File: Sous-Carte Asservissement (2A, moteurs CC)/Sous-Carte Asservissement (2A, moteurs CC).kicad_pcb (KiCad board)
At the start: 2 copper layers, 6 parts, among them P1 CONN_01X18, P2 CONN_01X02, P3 CONN_01X02, P4 CONN_01X04, P5 CONN_01X04

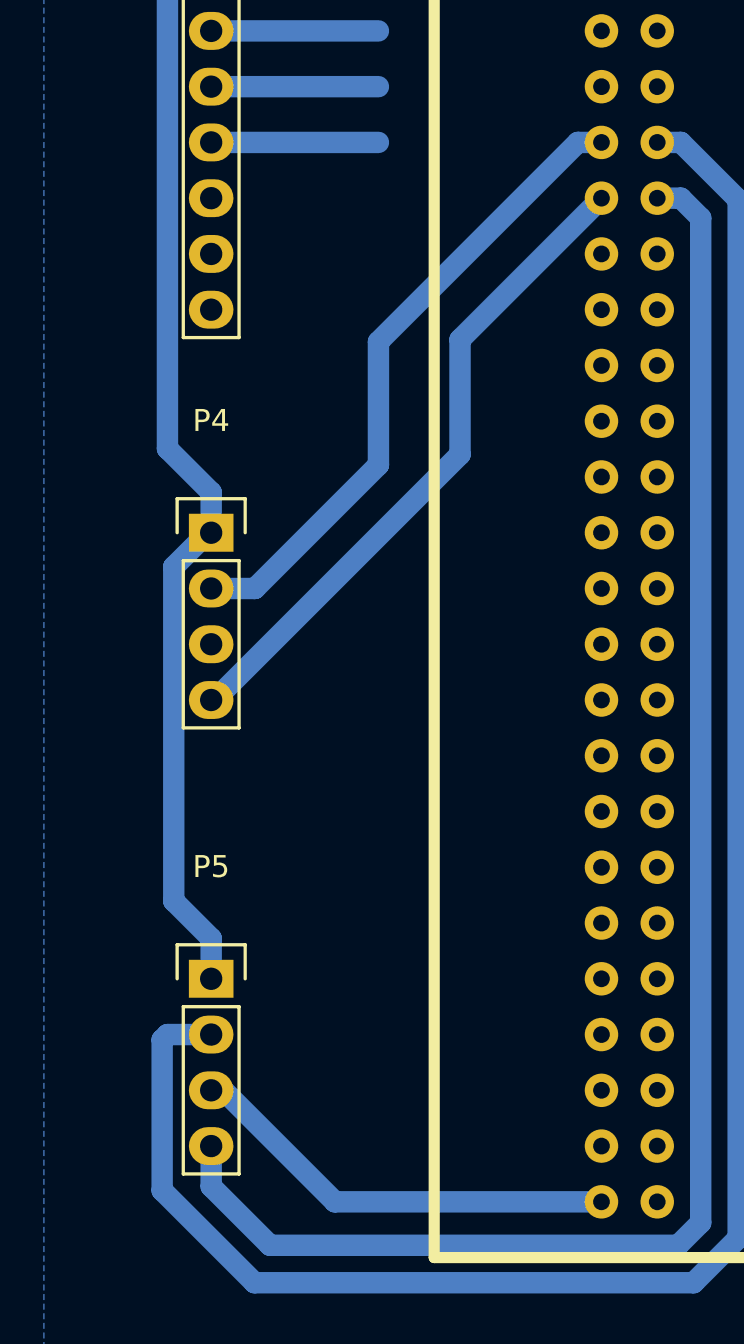
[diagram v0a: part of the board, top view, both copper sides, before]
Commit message: changé de timer un codeur
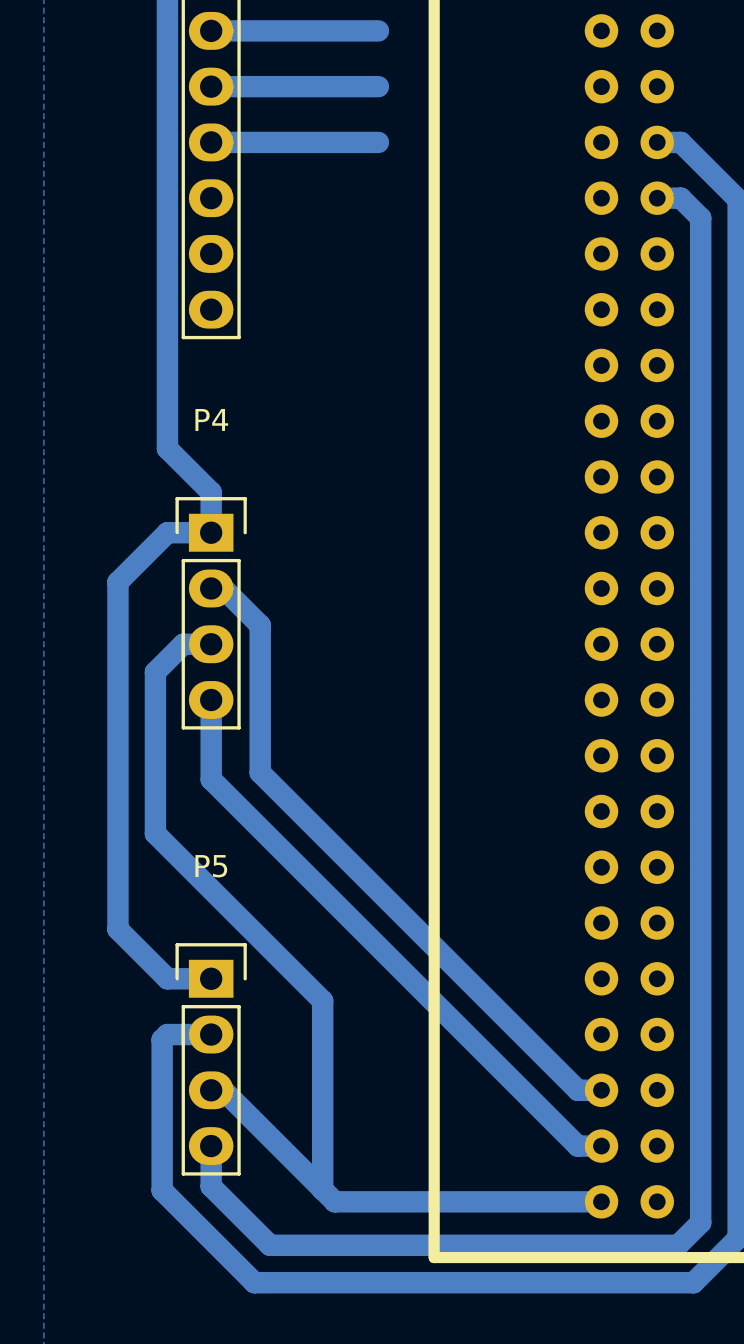
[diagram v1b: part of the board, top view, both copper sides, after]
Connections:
- P4 pad 2: TIM5_CH2 -> TIM4_CH2
- P4 pad 4: TIM5_CH4 -> TIM4_CH4
- stm321 pad 45: Net-(stm321-Pad45) -> TIM4_CH2
- stm321 pad 47: Net-(stm321-Pad47) -> TIM4_CH4
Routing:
- net TIM4_CH2: track 0.00 -> 31.2 mm
- net TIM5_CH4: track 30.3 -> 0.00 mm
- net GND: track 20.0 -> 49.8 mm
- net TIM5_CH2: track 29.5 -> 0.00 mm
- net TIM4_CH4: track 0.00 -> 28.5 mm
- net +5V: track 150.5 -> 155.0 mm

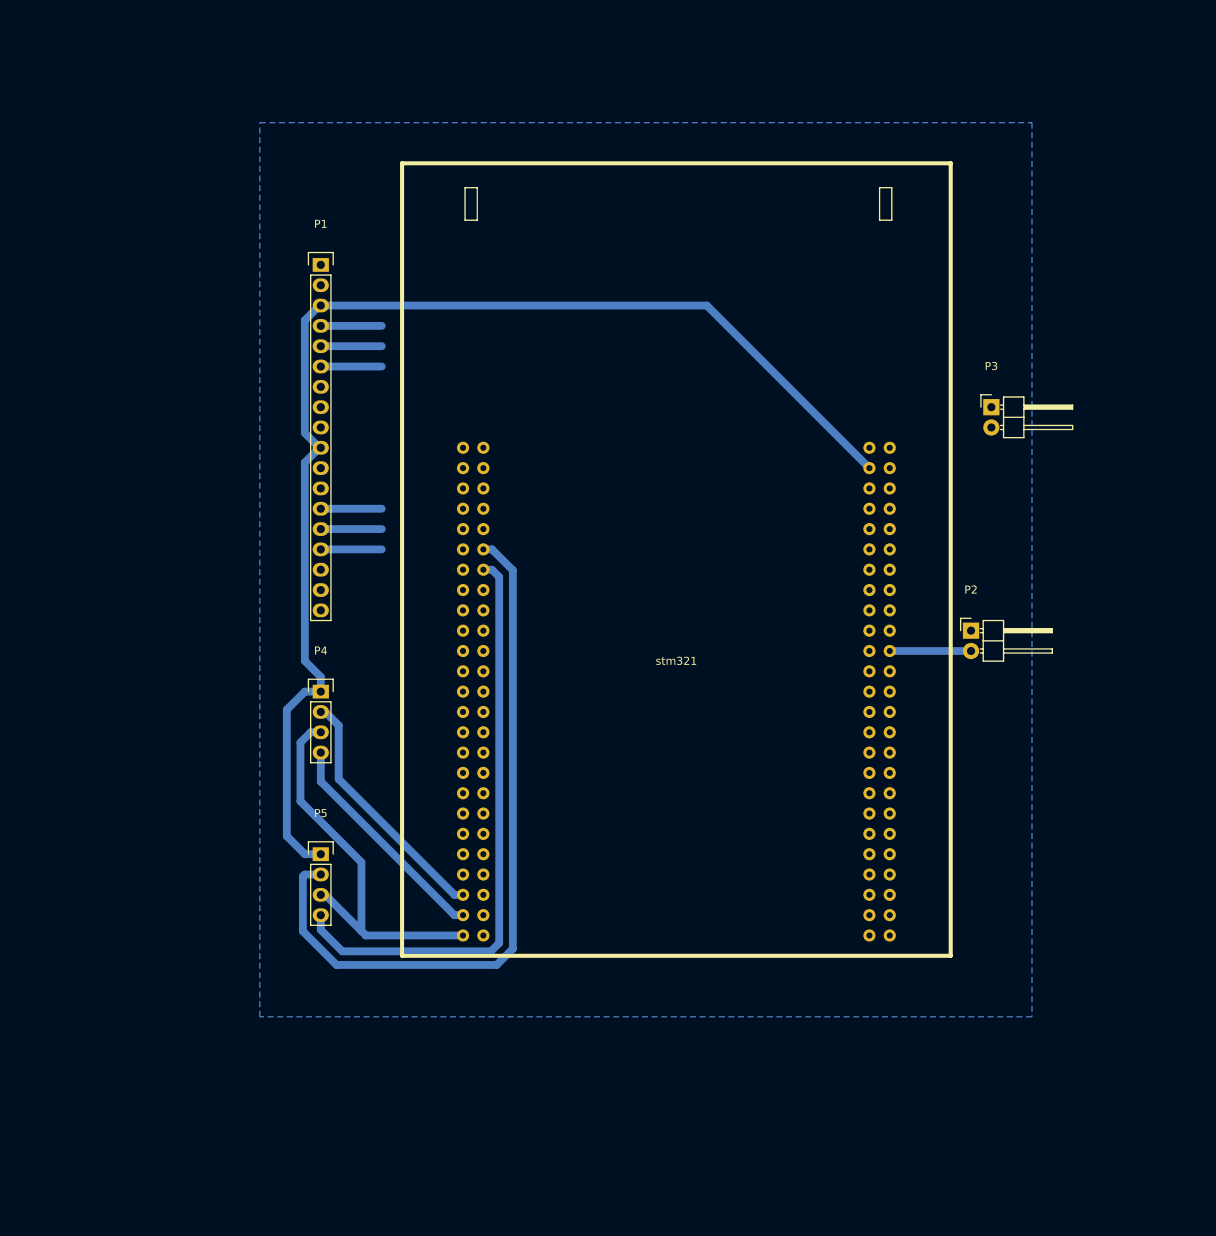
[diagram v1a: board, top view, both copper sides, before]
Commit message: Sous carte asser dite -- arraignée - avec pinoche et tout, routée
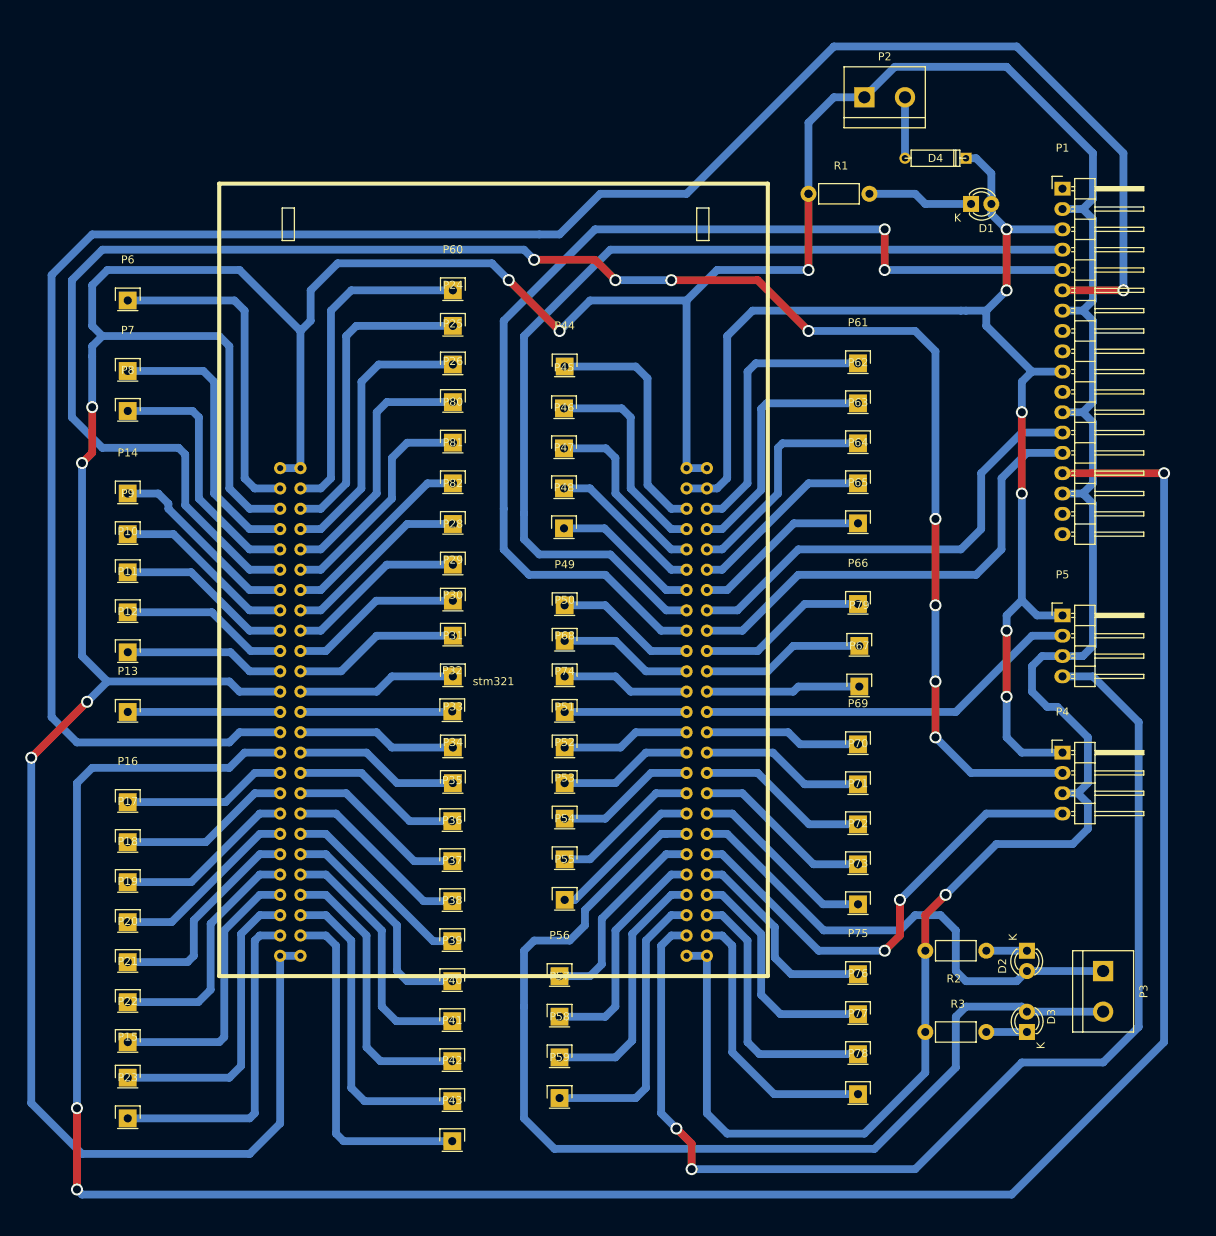
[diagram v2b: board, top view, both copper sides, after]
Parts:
- added D1: LED, LEDs:LED-3MM, F.Cu at (172.7, 55.9)
- added D2: LED, LEDs:LED-3MM, F.Cu at (179.7, 149.2)
- added D3: LED, LEDs:LED-3MM, F.Cu at (179.7, 159.4)
- added D4: D, Discret:D3, F.Cu at (168.3, 50.2)
- added P10: CONN_01X01, Pin_Headers:Pin_Header_Straight_1x01, F.Cu at (67.3, 101.9)
- added P11: CONN_01X01, Pin_Headers:Pin_Header_Straight_1x01, F.Cu at (67.3, 106.9)
- added P12: CONN_01X01, Pin_Headers:Pin_Header_Straight_1x01, F.Cu at (67.3, 111.9)
- added P13: CONN_01X01, Pin_Headers:Pin_Header_Straight_1x01, F.Cu at (67.3, 119.4)
- added P14: CONN_01X01, Pin_Headers:Pin_Header_Straight_1x01, F.Cu at (67.3, 92.1)
- added P15: CONN_01X01, Pin_Headers:Pin_Header_Straight_1x01, F.Cu at (67.3, 165.1)
- added P16: CONN_01X01, Pin_Headers:Pin_Header_Straight_1x01, F.Cu at (67.3, 130.6)
- added P17: CONN_01X01, Pin_Headers:Pin_Header_Straight_1x01, F.Cu at (67.3, 135.6)
- added P18: CONN_01X01, Pin_Headers:Pin_Header_Straight_1x01, F.Cu at (67.3, 140.6)
- added P19: CONN_01X01, Pin_Headers:Pin_Header_Straight_1x01, F.Cu at (67.3, 145.6)
- added P20: CONN_01X01, Pin_Headers:Pin_Header_Straight_1x01, F.Cu at (67.3, 150.6)
- added P21: CONN_01X01, Pin_Headers:Pin_Header_Straight_1x01, F.Cu at (67.3, 155.6)
- added P22: CONN_01X01, Pin_Headers:Pin_Header_Straight_1x01, F.Cu at (67.3, 160.6)
- added P23: CONN_01X01, Pin_Headers:Pin_Header_Straight_1x01, F.Cu at (67.3, 170.2)
- added P24: CONN_01X01, Pin_Headers:Pin_Header_Straight_1x01, F.Cu at (108.0, 71.1)
- added P25: CONN_01X01, Pin_Headers:Pin_Header_Straight_1x01, F.Cu at (108.0, 76.0)
- added P26: CONN_01X01, Pin_Headers:Pin_Header_Straight_1x01, F.Cu at (108.0, 80.6)
- added P28: CONN_01X01, Pin_Headers:Pin_Header_Straight_1x01, F.Cu at (108.0, 101.0)
- added P29: CONN_01X01, Pin_Headers:Pin_Header_Straight_1x01, F.Cu at (108.0, 105.5)
- added P30: CONN_01X01, Pin_Headers:Pin_Header_Straight_1x01, F.Cu at (108.0, 109.9)
- added P31: CONN_01X01, Pin_Headers:Pin_Header_Straight_1x01, F.Cu at (108.0, 114.9)
- added P32: CONN_01X01, Pin_Headers:Pin_Header_Straight_1x01, F.Cu at (107.9, 119.3)
- added P33: CONN_01X01, Pin_Headers:Pin_Header_Straight_1x01, F.Cu at (108.0, 123.8)
- added P34: CONN_01X01, Pin_Headers:Pin_Header_Straight_1x01, F.Cu at (108.0, 128.3)
- added P35: CONN_01X01, Pin_Headers:Pin_Header_Straight_1x01, F.Cu at (107.9, 133.0)
- added P36: CONN_01X01, Pin_Headers:Pin_Header_Straight_1x01, F.Cu at (107.9, 138.0)
- added P37: CONN_01X01, Pin_Headers:Pin_Header_Straight_1x01, F.Cu at (107.9, 143.0)
- added P38: CONN_01X01, Pin_Headers:Pin_Header_Straight_1x01, F.Cu at (107.9, 148.0)
- added P39: CONN_01X01, Pin_Headers:Pin_Header_Straight_1x01, F.Cu at (107.9, 153.0)
- added P40: CONN_01X01, Pin_Headers:Pin_Header_Straight_1x01, F.Cu at (107.9, 158.0)
- added P41: CONN_01X01, Pin_Headers:Pin_Header_Straight_1x01, F.Cu at (107.9, 163.0)
- added P42: CONN_01X01, Pin_Headers:Pin_Header_Straight_1x01, F.Cu at (107.9, 168.0)
- added P43: CONN_01X01, Pin_Headers:Pin_Header_Straight_1x01, F.Cu at (107.9, 173.0)
- added P44: CONN_01X01, Pin_Headers:Pin_Header_Straight_1x01, F.Cu at (121.9, 76.2)
- added P45: CONN_01X01, Pin_Headers:Pin_Header_Straight_1x01, F.Cu at (121.8, 81.4)
- added P46: CONN_01X01, Pin_Headers:Pin_Header_Straight_1x01, F.Cu at (121.8, 86.4)
- added P47: CONN_01X01, Pin_Headers:Pin_Header_Straight_1x01, F.Cu at (121.8, 91.4)
- added P48: CONN_01X01, Pin_Headers:Pin_Header_Straight_1x01, F.Cu at (121.8, 96.4)
- added P49: CONN_01X01, Pin_Headers:Pin_Header_Straight_1x01, F.Cu at (121.9, 106.0)
- added P50: CONN_01X01, Pin_Headers:Pin_Header_Straight_1x01, F.Cu at (121.9, 110.5)
- added P51: CONN_01X01, Pin_Headers:Pin_Header_Straight_1x01, F.Cu at (121.9, 123.8)
- added P52: CONN_01X01, Pin_Headers:Pin_Header_Straight_1x01, F.Cu at (121.9, 128.3)
- added P53: CONN_01X01, Pin_Headers:Pin_Header_Straight_1x01, F.Cu at (121.9, 132.7)
- added P54: CONN_01X01, Pin_Headers:Pin_Header_Straight_1x01, F.Cu at (121.9, 137.8)
- added P55: CONN_01X01, Pin_Headers:Pin_Header_Straight_1x01, F.Cu at (121.9, 142.9)
- added P56: CONN_01X01, Pin_Headers:Pin_Header_Straight_1x01, F.Cu at (121.3, 152.4)
- added P57: CONN_01X01, Pin_Headers:Pin_Header_Straight_1x01, F.Cu at (121.3, 157.5)
- added P58: CONN_01X01, Pin_Headers:Pin_Header_Straight_1x01, F.Cu at (121.3, 162.6)
- added P59: CONN_01X01, Pin_Headers:Pin_Header_Straight_1x01, F.Cu at (121.3, 167.6)
- added P6: CONN_01X01, Pin_Headers:Pin_Header_Straight_1x01, F.Cu at (67.3, 67.9)
- added P60: CONN_01X01, Pin_Headers:Pin_Header_Straight_1x01, F.Cu at (108.0, 66.7)
- added P61: CONN_01X01, Pin_Headers:Pin_Header_Straight_1x01, F.Cu at (158.6, 75.8)
- added P62: CONN_01X01, Pin_Headers:Pin_Header_Straight_1x01, F.Cu at (158.6, 80.8)
- added P63: CONN_01X01, Pin_Headers:Pin_Header_Straight_1x01, F.Cu at (158.6, 85.8)
- added P64: CONN_01X01, Pin_Headers:Pin_Header_Straight_1x01, F.Cu at (158.6, 90.8)
- added P65: CONN_01X01, Pin_Headers:Pin_Header_Straight_1x01, F.Cu at (158.6, 95.8)
- added P66: CONN_01X01, Pin_Headers:Pin_Header_Straight_1x01, F.Cu at (158.6, 105.9)
- added P67: CONN_01X01, Pin_Headers:Pin_Header_Straight_1x01, F.Cu at (158.8, 116.2)
- added P68: CONN_01X01, Pin_Headers:Pin_Header_Straight_1x01, F.Cu at (121.9, 114.9)
- added P69: CONN_01X01, Pin_Headers:Pin_Header_Straight_1x01, F.Cu at (158.6, 123.4)
- added P7: CONN_01X01, Pin_Headers:Pin_Header_Straight_1x01, F.Cu at (67.3, 76.8)
- added P70: CONN_01X01, Pin_Headers:Pin_Header_Straight_1x01, F.Cu at (158.6, 128.4)
- added P71: CONN_01X01, Pin_Headers:Pin_Header_Straight_1x01, F.Cu at (158.6, 133.4)
- added P72: CONN_01X01, Pin_Headers:Pin_Header_Straight_1x01, F.Cu at (158.6, 138.4)
- added P73: CONN_01X01, Pin_Headers:Pin_Header_Straight_1x01, F.Cu at (158.6, 143.4)
- added P74: CONN_01X01, Pin_Headers:Pin_Header_Straight_1x01, F.Cu at (121.9, 119.4)
- added P75: CONN_01X01, Pin_Headers:Pin_Header_Straight_1x01, F.Cu at (158.6, 152.2)
- added P76: CONN_01X01, Pin_Headers:Pin_Header_Straight_1x01, F.Cu at (158.6, 157.2)
- added P77: CONN_01X01, Pin_Headers:Pin_Header_Straight_1x01, F.Cu at (158.6, 162.2)
- added P78: CONN_01X01, Pin_Headers:Pin_Header_Straight_1x01, F.Cu at (158.6, 167.2)
- added P79: CONN_01X01, Pin_Headers:Pin_Header_Straight_1x01, F.Cu at (158.8, 111.1)
- added P8: CONN_01X01, Pin_Headers:Pin_Header_Straight_1x01, F.Cu at (67.3, 81.8)
- added P80: CONN_01X01, Pin_Headers:Pin_Header_Straight_1x01, F.Cu at (108.0, 85.7)
- added P81: CONN_01X01, Pin_Headers:Pin_Header_Straight_1x01, F.Cu at (108.0, 90.8)
- added P82: CONN_01X01, Pin_Headers:Pin_Header_Straight_1x01, F.Cu at (108.0, 95.9)
- added P9: CONN_01X01, Pin_Headers:Pin_Header_Straight_1x01, F.Cu at (67.3, 97.2)
- added R1: 150, Resistors_ThroughHole:Resistor_Horizontal_RM7mm, F.Cu at (152.4, 54.6)
- added R2: 150, Resistors_ThroughHole:Resistor_Horizontal_RM7mm, F.Cu at (174.6, 149.2)
- added R3: 150, Resistors_ThroughHole:Resistor_Horizontal_RM7mm, F.Cu at (167.0, 159.4)
- P1: footprint Pin_Headers:Pin_Header_Straight_1x18 -> Pin_Headers:Pin_Header_Angled_1x18
- P2, P3: footprint Pin_Headers:Pin_Header_Angled_1x02 -> Connect:bornier2
- P4, P5: footprint Pin_Headers:Pin_Header_Straight_1x04 -> Pin_Headers:Pin_Header_Angled_1x04
- moved P5 97.4 mm to (184.2, 107.3)
- moved P1 93.2 mm to (184.2, 54.0)
- moved P4 93.0 mm to (184.2, 124.5)
- moved P3 74.3 mm to (189.2, 154.3), turned to 270 degrees
- moved P2 67.5 mm to (161.9, 42.5)
- moved stm321 23.0 mm to (86.4, 88.9)
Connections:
- P2 pad 2: +BATT -> Net-(D4-Pad2)
- P4 pad 2: TIM4_CH2 -> TIM2_CH2
- P4 pad 4: TIM4_CH4 -> TIM2_CH1
- P5 pad 2: TIM5_CH1 -> TIM3_CH2
- P5 pad 4: TIM5_CH3 -> TIM3_CH1
- stm321 pad 11: TIM5_CH2 -> TIM2_CH2
- stm321 pad 12: TIM5_CH1 -> Net-(P80-Pad1)
- stm321 pad 13: TIM5_CH4 -> Net-(P14-Pad1)
- stm321 pad 14: TIM5_CH3 -> Net-(P81-Pad1)
- stm321 pad 27: Net-(stm321-Pad27) -> M1PWM
- stm321 pad 29: Net-(stm321-Pad29) -> M2PWM
- stm321 pad 45: TIM4_CH2 -> Net-(P15-Pad1)
- stm321 pad 47: TIM4_CH4 -> Net-(P23-Pad1)
- stm321 pad 65: Net-(stm321-Pad65) -> M1I2
- stm321 pad 66: Net-(stm321-Pad66) -> M2_I2
- stm321 pad 67: Net-(stm321-Pad67) -> M1I1
- stm321 pad 68: Net-(stm321-Pad68) -> M2_I1
- stm321 pad 72: +BATT -> Net-(P79-Pad1)
- stm321 pad 76: Net-(stm321-Pad76) -> TIM3_CH2
- stm321 pad 87: Net-(stm321-Pad87) -> UART_TX
- stm321 pad 88: Net-(stm321-Pad88) -> UART_RX
- stm321 pad 90: Net-(stm321-Pad90) -> TIM2_CH1
- stm321 pad 97: Net-(stm321-Pad97) -> TIM3_CH1
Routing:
- net GND: track 49.8 -> 651.7 mm, vias 0 -> 9
- net M2PWM: track 7.62 -> 305.6 mm, vias 0 -> 3
- net M1PWM: track 7.62 -> 261.8 mm, vias 0 -> 1
- net TIM2_CH2: track 0.00 -> 235.6 mm, vias 0 -> 8
- net TIM3_CH1: track 0.00 -> 146.5 mm, vias 0 -> 2
- net UART_TX: track 0.00 -> 133.8 mm
- net M1I1: track 7.62 -> 135.3 mm, vias 0 -> 2
- net M1I2: track 7.62 -> 121.2 mm
- net TIM5_CH1: track 90.1 -> 0.00 mm
- net TIM5_CH3: track 73.8 -> 0.00 mm
- net UART_RX: track 0.00 -> 62.2 mm
- net TIM2_CH1: track 0.00 -> 59.2 mm, vias 0 -> 2
- net M2_I1: track 7.62 -> 58.9 mm
- net M2_I2: track 7.62 -> 57.7 mm
- net TIM3_CH2: track 0.00 -> 48.4 mm
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- removed copper zone on B.Cu, net GND

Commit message: Ajout pin_header Uart Asser
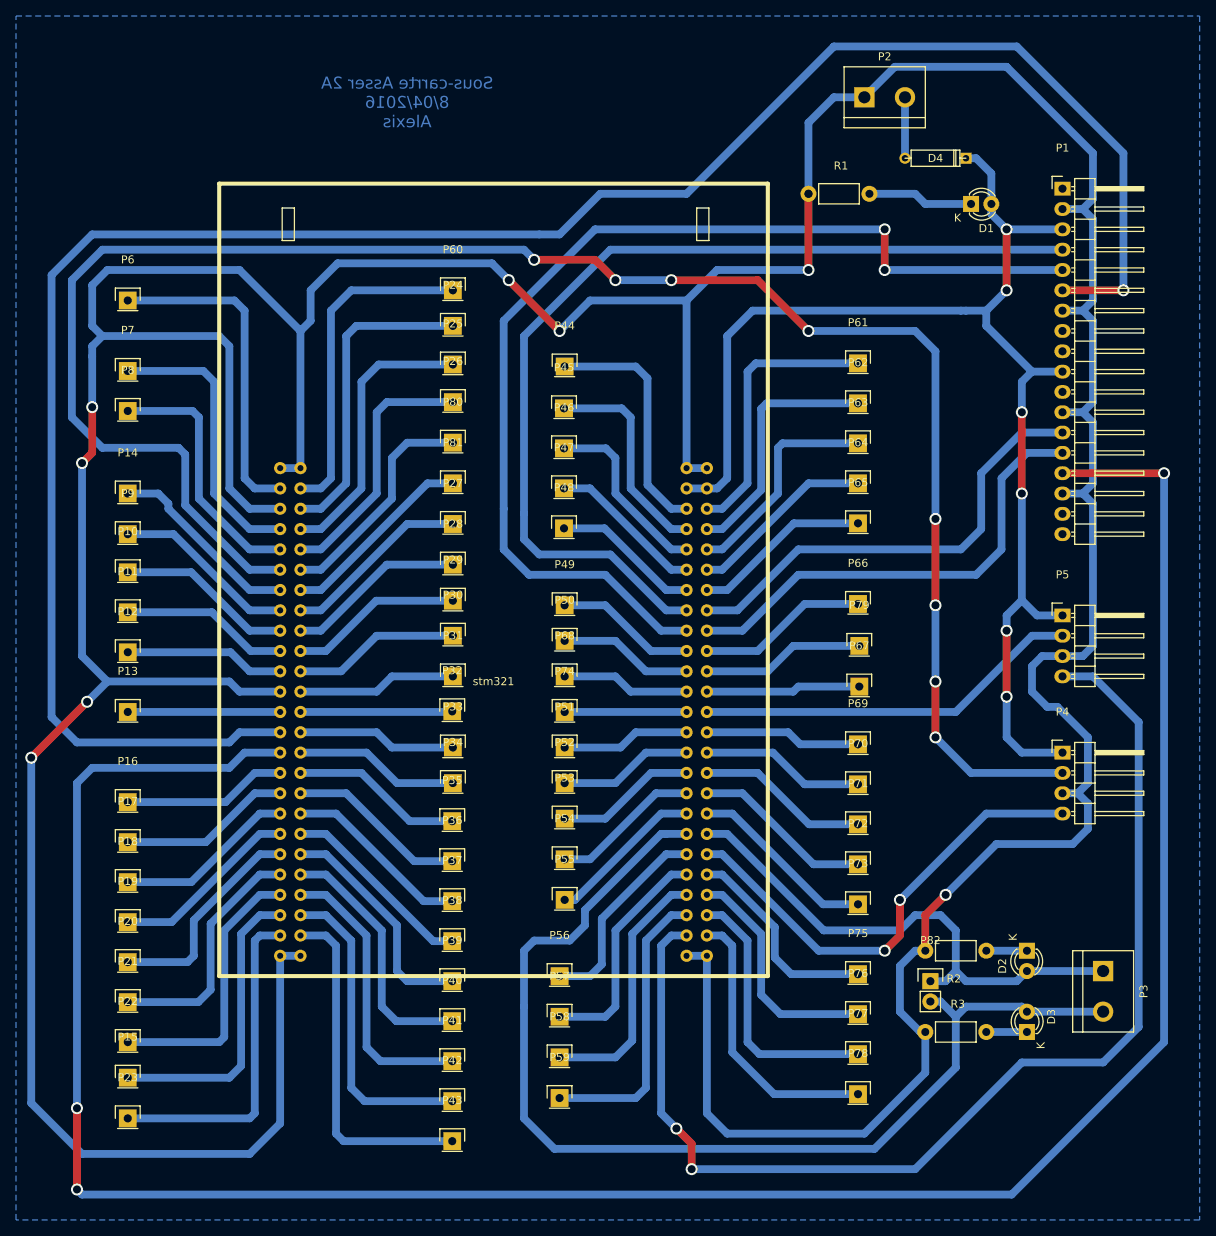
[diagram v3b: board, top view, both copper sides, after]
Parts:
- added P27: CONN_01X01, Pin_Headers:Pin_Header_Straight_1x01, F.Cu at (108.0, 95.9)
- P82: value CONN_01X01 -> CONN_01X02; footprint Pin_Headers:Pin_Header_Straight_1x01 -> Pin_Headers:Pin_Header_Straight_1x02
- moved P82 82.6 mm to (167.6, 153.0)
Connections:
- P82 pad 1: Net-(P27-Pad1) -> UART_RX
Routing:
- net UART_TX: track 133.8 -> 137.7 mm
- net GND: track 651.7 -> 655.5 mm
- net UART_RX: track 62.2 -> 65.9 mm
- added copper zone on B.Cu, net GND
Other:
- board text added: "Sous-carrte Asser 2A 8/04/2016 Alexis"
